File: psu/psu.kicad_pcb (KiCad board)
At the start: 2 copper layers, 100 x 100 mm, 134 parts, among them IC101 TSR 1-24150, IC102 STM32F334K8T6, IC103 TSR 1-2450, IC104 NCP161, IC201 INA139, IC202 AD8605, IC203 MCP1416, IC204 AD8065, IC205 INA139, IC206 AD8605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

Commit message: More PCB
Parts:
- moved C223 9.89 mm to (175.5, 103.8), turned to 270 degrees
- moved R228 9.39 mm to (180.0, 100.0), turned to 180 degrees
- moved C224 8.07 mm to (177.2, 103.8), turned to 270 degrees
- moved TP205 5.40 mm to (178.5, 114.8)
- moved IC205 5.01 mm to (180.0, 103.8), turned to 90 degrees
- moved D101 1.00 mm to (112.0, 122.0)
- moved D109 1.00 mm to (189.0, 120.0)
- moved D110 1.00 mm to (189.0, 123.0)
- moved D111 1.00 mm to (189.0, 126.5)
- moved R109 1.00 mm to (186.5, 125.5)
- moved R110 1.00 mm to (189.0, 121.5)
- moved R111 1.00 mm to (189.0, 124.5)
- moved D112 0.50 mm to (185.0, 133.5)
- moved D113 0.50 mm to (185.0, 135.0)
- moved D114 0.50 mm to (185.0, 138.0)
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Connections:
- net Net-(C223-Pad2) renamed /Flyback/390V
- TP205 pad 1: Net-(C227-Pad1) -> /I_OUT
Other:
- outline, holes or cut-outs redrawn
- board text added: "+"
- board text added: "-"
- board text added: "0V"
- board text added: "15V"
- board text added: "2019-08-27 r1 AG"
- board text added: "24V"
- board text added: "24V ~EN~ TX 0V"
- board text added: "24VDC 2.5A"
- board text added: "3V TX RX 0V"
- board text added: "3V3"
- board text added: "400V"
- board text added: "400V HV PSU"
- board text added: "5V"
- board text added: "CTRL"
- board text added: "Capacitors remain energised up to 1min after disconnection. Ensure they are discharged!"
- board text added: "ERR"
- board text added: "GD"
- board text added: "HIGH VOLTAGE"
- board text added: "IIN"
- board text added: "IOUT"
- board text added: "IQ"
- board text added: "VOUT"
- board text added: "VQ"

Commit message: More pcb layout
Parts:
- added G***: LOGO, psu:hv, F.Cu at (196.0, 95.0)
- added G***: LOGO, psu:hv, F.Cu at (196.0, 124.0)
- TP102, TP202, TP203, TP206, TP207: footprint agg:SIL-254P-01 -> agg:KEYSTONE5016
- moved C103 97.2 mm to (129.5, 66.0), turned to 270 degrees
- moved C104 95.6 mm to (124.2, 67.5), turned to 90 degrees
- moved Y101 93.7 mm to (127.0, 66.0), turned to 270 degrees
- moved D103 93.2 mm to (161.5, 61.5)
- moved R101 93.2 mm to (161.5, 57.5)
- moved TP101 93.2 mm to (161.5, 54.5)
- moved TP102 93.2 mm to (156.5, 57.5), turned to 180 degrees
- moved D104 93.1 mm to (166.2, 61.5)
- moved R104 93.1 mm to (166.2, 57.5)
- moved TP103 93.1 mm to (166.2, 54.5)
- moved D105 93.0 mm to (171.0, 61.5)
- moved R105 93.0 mm to (171.0, 57.5)
- moved TP104 93.0 mm to (171.0, 54.5)
- moved D108 92.9 mm to (175.8, 61.5)
- moved R108 92.9 mm to (175.8, 57.5)
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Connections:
- TP202 pad 1: /GD -> Net-(IC203-Pad5)
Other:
- outline, holes or cut-outs redrawn
- board text added: "Capacitors remain energised up to 1min after disconnection."
- board text removed: "CTRL"
- board text removed: "Capacitors remain energised up to 1min after disconnection. Ensure they are discharged!"

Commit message: routing
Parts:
- moved R102 58.5 mm to (107.0, 91.0), turned to 0 degrees
- moved R103 55.8 mm to (107.0, 89.0), turned to 180 degrees
- moved C101 52.4 mm to (109.5, 90.0), turned to 270 degrees
- moved J103 4.00 mm to (195.2, 132.0)
- moved D204 2.06 mm to (185.5, 126.5)
- moved D205 2.06 mm to (189.0, 126.5)
- moved D103 1.75 mm to (161.5, 63.2)
- moved D104 1.75 mm to (166.2, 63.2)
- moved D105 1.75 mm to (171.0, 63.2)
- moved D106 1.75 mm to (185.2, 63.2)
- moved D107 1.75 mm to (180.5, 63.0)
- moved D108 1.75 mm to (175.8, 63.2)
- moved R101 1.75 mm to (161.5, 59.2)
- moved R104 1.75 mm to (166.2, 59.2)
- moved R105 1.75 mm to (171.0, 59.2)
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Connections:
- net Net-(C216-Pad2) renamed /Flyback/400V
- IC102 pad 12: /VQ -> /V_Q
- IC102 pad 14: /VQ -> /V_Q
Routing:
- net GND: track 0.00 -> 258.7 mm, vias 0 -> 86
- net 24v: track 0.00 -> 156.4 mm
- net 3v3: track 0.00 -> 101.4 mm
- net /I_OUT: track 0.00 -> 85.4 mm
- net Net-(C206-Pad2): track 0.00 -> 72.8 mm
- net Net-(C214-Pad2): track 0.00 -> 62.0 mm
- net /Flyback/400V: track 0.00 -> 58.6 mm
- net /V_Q: track 0.00 -> 52.1 mm
- net /I_Q: track 0.00 -> 42.5 mm
- net /I_IN: track 0.00 -> 39.7 mm
- net /Flyback/390V: track 0.00 -> 35.8 mm, vias 0 -> 2
- net /VIN_MON: track 0.00 -> 30.6 mm
- net 5v: track 0.00 -> 30.0 mm
- net Net-(D101-Pad1): track 0.00 -> 23.4 mm
- net /Flyback/HV+: track 0.00 -> 20.8 mm
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- added copper zone on B.Cu, net GND
- added copper zone on F.Cu, net GND
- added copper zone on F.Cu, net Net-(C206-Pad2)
- added copper zone on F.Cu, net Net-(C214-Pad2)
- added copper zone on F.Cu, net Net-(Q201-PadS)
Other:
- outline, holes or cut-outs redrawn
- rule trace_min: 0.2 -> 0.15
- rule via_min_size: 0.4 -> 0.6

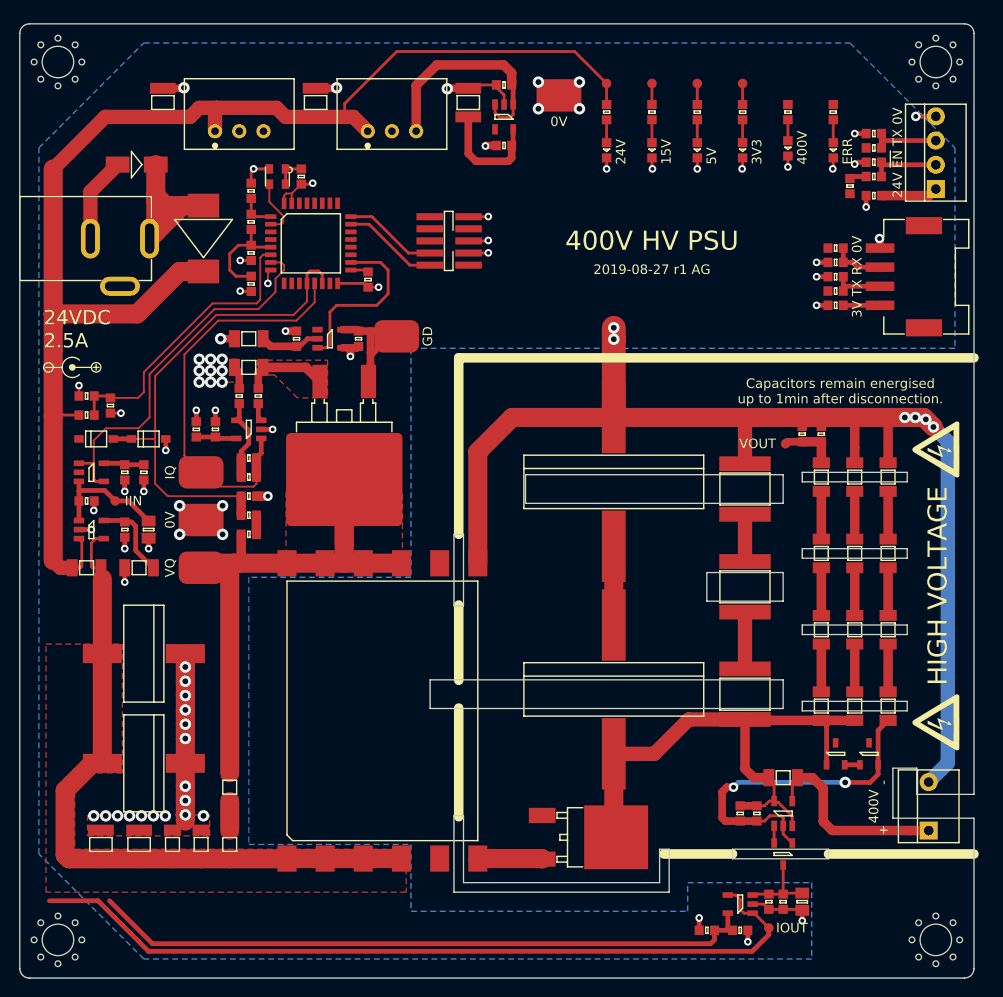
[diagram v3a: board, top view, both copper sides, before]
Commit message: Complete routing. But maybe the transformer is the wrong way around.
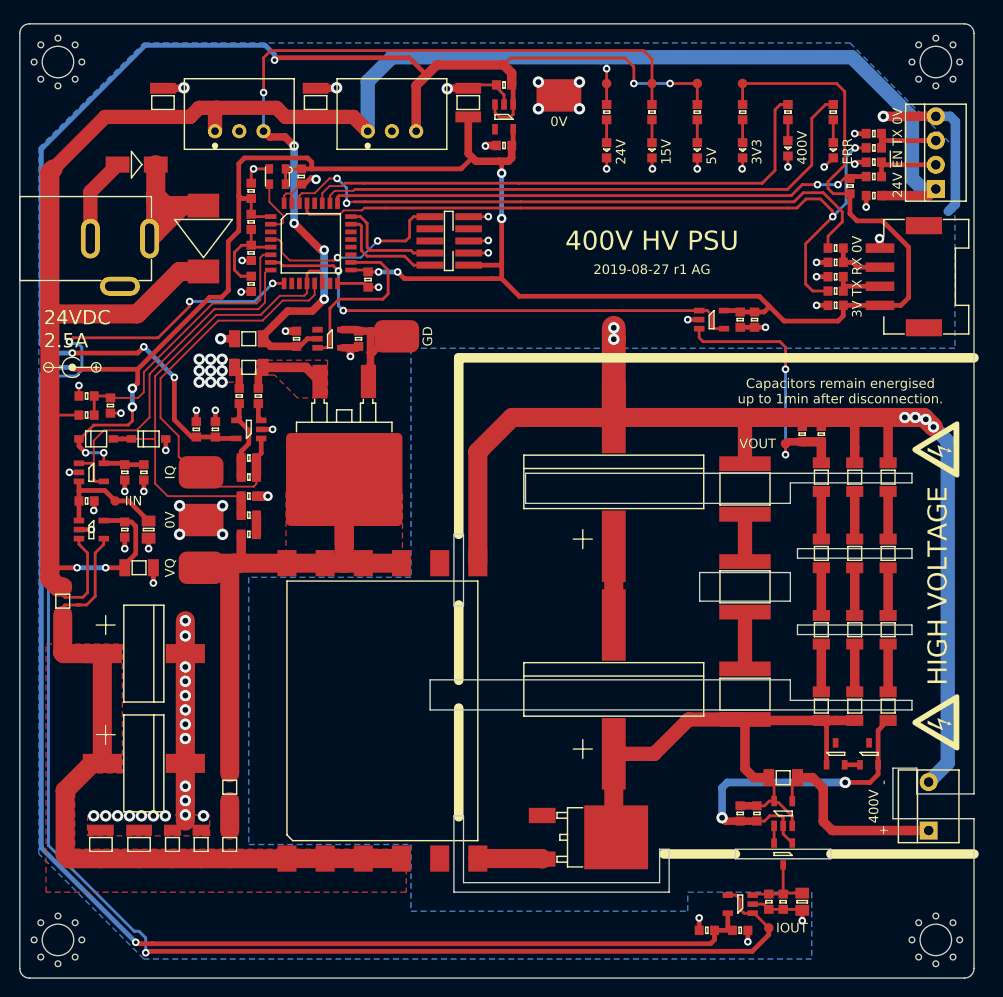
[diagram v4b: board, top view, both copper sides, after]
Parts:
- added C228: 100n, agg:0603, F.Cu at (175.5, 81.0)
- added C229: 1µ, agg:0603, F.Cu at (177.0, 81.0)
- added IC207: AD8605, agg:SOT-23-5, F.Cu at (172.5, 81.0)
- moved C214 6.00 mm to (122.0, 136.0)
- moved R204 6.00 mm to (122.0, 130.0)
- moved R201 4.30 mm to (104.5, 110.5), turned to 270 degrees
- turned C201 to 0 degrees
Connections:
- C214 pad 1: Net-(C214-Pad1) -> Net-(C206-Pad2)
- C222 pad 1: /VOUT_MON -> Net-(C222-Pad1)
- IC102 pad 26: /LED_STAT -> /LED_FAULT
- IC102 pad 27: /LED_FAULT -> /LED_STAT
- IC102 pad 7: /I_IN -> /VOUT_MON
- IC102 pad 8: /VOUT_MON -> /I_IN
- Q201 pad D: Net-(C214-Pad2) -> Net-(Q201-PadD)
- R204 pad 1: Net-(C206-Pad2) -> Net-(C214-Pad2)
- R204 pad 2: Net-(C214-Pad1) -> Net-(Q201-PadD)
- R206 pad 1: Net-(C214-Pad2) -> Net-(Q201-PadD)
- R216 pad 2: /VOUT_MON -> Net-(C222-Pad1)
- R217 pad 1: /VOUT_MON -> Net-(C222-Pad1)
- T201 pad 10: Net-(C214-Pad2) -> Net-(Q201-PadD)
- T201 pad 11: Net-(C214-Pad2) -> Net-(Q201-PadD)
- T201 pad 12: Net-(C214-Pad2) -> Net-(Q201-PadD)
- T201 pad 9: Net-(C214-Pad2) -> Net-(Q201-PadD)
- TP204 pad 1: /VOUT_MON -> Net-(C222-Pad1)
- TP207 pad 1: Net-(C214-Pad2) -> Net-(Q201-PadD)
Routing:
- net 3v3: track 101.4 -> 360.0 mm, vias 0 -> 10
- net 5v: track 30.0 -> 143.3 mm, vias 0 -> 6
- net /I_OUT: track 85.4 -> 170.9 mm, vias 0 -> 4
- net 15v: track 8.56 -> 90.0 mm, vias 0 -> 5
- net /UART_TX: track 0.00 -> 78.1 mm, vias 0 -> 2
- net /UART_RX: track 0.00 -> 66.2 mm, vias 0 -> 2
- net Net-(Q201-PadD): track 0.00 -> 62.0 mm
- net 24v: track 156.4 -> 217.0 mm, vias 0 -> 3
- net /LED_FAULT: track 0.00 -> 60.4 mm
- net Net-(C214-Pad2): track 62.0 -> 3.00 mm
- net /LED_STAT: track 0.00 -> 57.4 mm
- net /~RUN: track 1.78 -> 56.9 mm, vias 0 -> 2
- net /VOUT_MON: track 7.56 -> 53.2 mm, vias 1 -> 2
- net Net-(C222-Pad1): track 0.00 -> 28.8 mm, vias 0 -> 2
- net GND: track 258.7 -> 283.1 mm, vias 86 -> 91
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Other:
- outline, holes or cut-outs redrawn
- net class MV added: clearance 0.35, trace_width 0.25, via_dia 0.8, via_drill 0.4
- rule pad_to_mask_clearance: 0.051 -> 0.03

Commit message: Complete routing take 2, with transformer secondary pins swapped
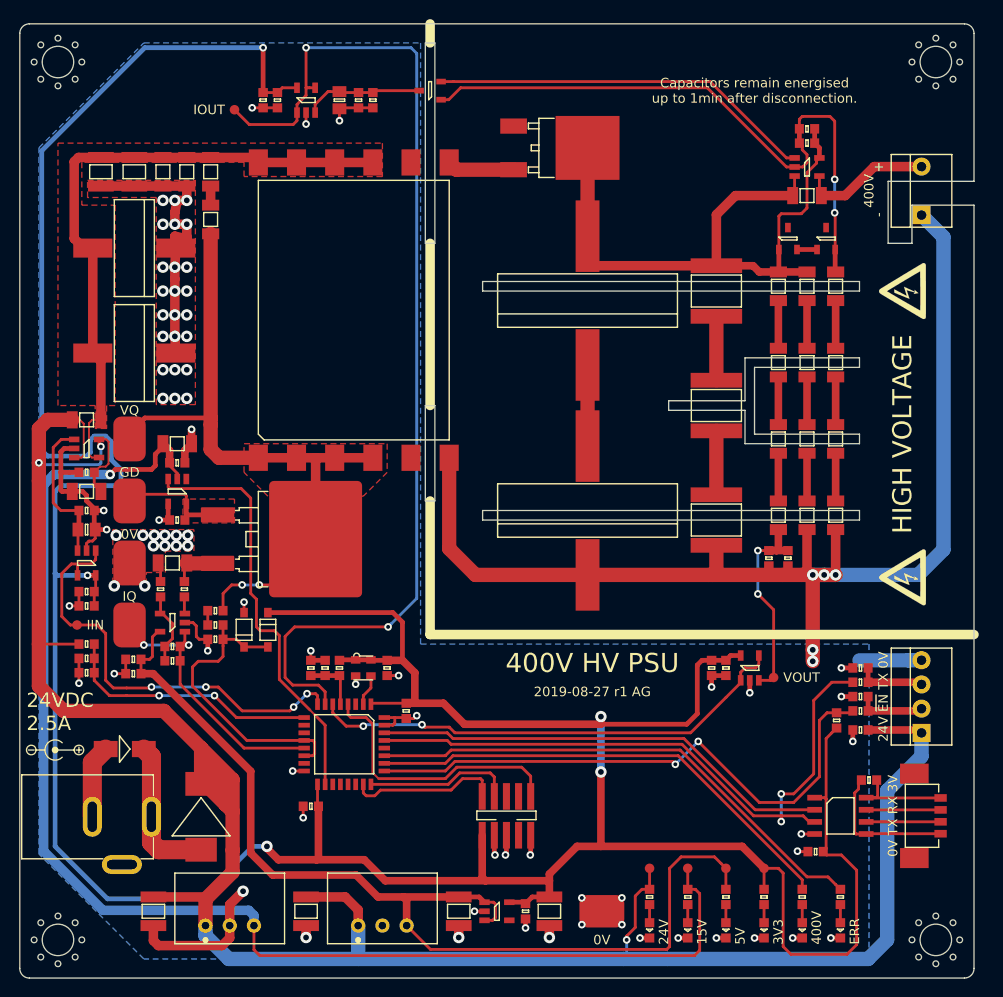
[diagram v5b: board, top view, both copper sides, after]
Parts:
- removed D112, D113, D114: ESD_DIODE, agg:0603
- removed G*** (x2): LOGO, psu:hv
- removed R112, R113: 1k, agg:0603
- added C112: 100n, agg:0603, F.Cu at (183.4, 136.8)
- added C113: 100n, agg:0603, F.Cu at (189.0, 129.2)
- added IC105: ADuM1201, agg:SOIC-8, F.Cu at (186.0, 133.0)
- added X106: HV SIGN, psu:hv, F.Cu at (192.5, 78.0)
- added X107: HV SIGN, psu:hv, F.Cu at (192.5, 108.0)
- C110: value 1µ -> 10µ; footprint agg:0603 -> agg:1210
- J104: footprint agg:SM04B-PASS -> agg:MOLEX-PICOBLADE-53398-0471
- moved TP205 102.4 mm to (122.5, 59.0)
- moved C226 100.3 mm to (125.5, 58.0), turned to 270 degrees
- moved C225 97.9 mm to (127.0, 58.0), turned to 270 degrees
- moved C227 97.0 mm to (133.5, 58.0)
- moved IC206 95.8 mm to (130.0, 58.0), turned to 90 degrees
- moved R227 95.1 mm to (135.5, 58.0)
- moved R226 93.7 mm to (137.0, 58.0)
- moved Q202 88.1 mm to (143.0, 57.0), turned to 180 degrees
- moved C110 86.7 mm to (146.0, 143.0), turned to 270 degrees
- moved TP102 85.6 mm to (161.0, 143.0), turned to 0 degrees
- moved C102 85.2 mm to (155.5, 143.0), turned to 270 degrees
- moved C106 84.8 mm to (114.0, 143.0), turned to 270 degrees
- moved C109 84.8 mm to (130.0, 143.0), turned to 270 degrees
- moved IC101 83.3 mm to (122.0, 144.5)
- moved IC103 83.3 mm to (138.0, 144.5)
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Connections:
- IC102 pad 26: /LED_FAULT -> /LED_STAT
- IC102 pad 27: /LED_STAT -> /LED_FAULT
- IC102 pad 6: /VIN_MON -> /VOUT_MON
- IC102 pad 7: /VOUT_MON -> /I_OUT
- IC102 pad 9: /I_OUT -> /VIN_MON
- J103 pad 1: /Flyback/HV+ -> GND
- J103 pad 3: GND -> /Flyback/HV+
- J104 pad 1: 3v3 -> Net-(C113-Pad1)
- J104 pad 4: GND -> Net-(C113-Pad2)
- T201 pad 1: Net-(C206-Pad2) -> Net-(Q201-PadD)
- T201 pad 10: Net-(Q201-PadD) -> Net-(C206-Pad2)
- T201 pad 11: Net-(Q201-PadD) -> Net-(C206-Pad2)
- T201 pad 12: Net-(Q201-PadD) -> Net-(C206-Pad2)
- T201 pad 2: Net-(C206-Pad2) -> Net-(Q201-PadD)
- T201 pad 3: Net-(C206-Pad2) -> Net-(Q201-PadD)
- T201 pad 4: Net-(C206-Pad2) -> Net-(Q201-PadD)
- T201 pad 6: Net-(D203-Pad2) -> GND
- T201 pad 7: GND -> Net-(D203-Pad2)
- T201 pad 9: Net-(Q201-PadD) -> Net-(C206-Pad2)
- TP201 pad 1: Net-(C205-Pad1) -> /I_IN
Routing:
- net /I_OUT: track 170.9 -> 111.2 mm, vias 4 -> 2
- net 15v: track 90.0 -> 143.1 mm, vias 5 -> 1
- net Net-(IC205-Pad1): track 1.80 -> 40.4 mm
- net 5v: track 143.3 -> 109.9 mm, vias 6 -> 0
- net /Flyback/390V: track 36.1 -> 67.2 mm
- net 24v: track 217.0 -> 244.1 mm
- net /GD: track 18.7 -> 44.1 mm
- net /V_Q: track 51.5 -> 31.6 mm
- net /UART_RX: track 66.2 -> 48.4 mm, vias 2 -> 0
- net Net-(C113-Pad2): track 0.00 -> 14.9 mm
- net 3v3: track 360.0 -> 373.8 mm, vias 10 -> 5
- net /I_Q: track 42.7 -> 29.9 mm, vias 0 -> 2
- net Net-(C206-Pad2): track 78.4 -> 66.3 mm
- net Net-(C113-Pad1): track 0.00 -> 10.8 mm
- net /I_IN: track 37.3 -> 46.4 mm, vias 0 -> 4
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- added copper zone on F.Cu, net Net-(IC203-Pad5)
- added copper zone on F.Cu, net Net-(Q201-PadD)
- removed copper zone on F.Cu, net Net-(C214-Pad2)
- removed copper zone on F.Cu, net Net-(Q201-PadS)
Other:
- outline, holes or cut-outs redrawn
- net class Default: clearance 0.2 -> 0.25
- rule trace_clearance: 0.2 -> 0.25
- board text added: "0V TX RX 3V"
- board text removed: "3V TX RX 0V"

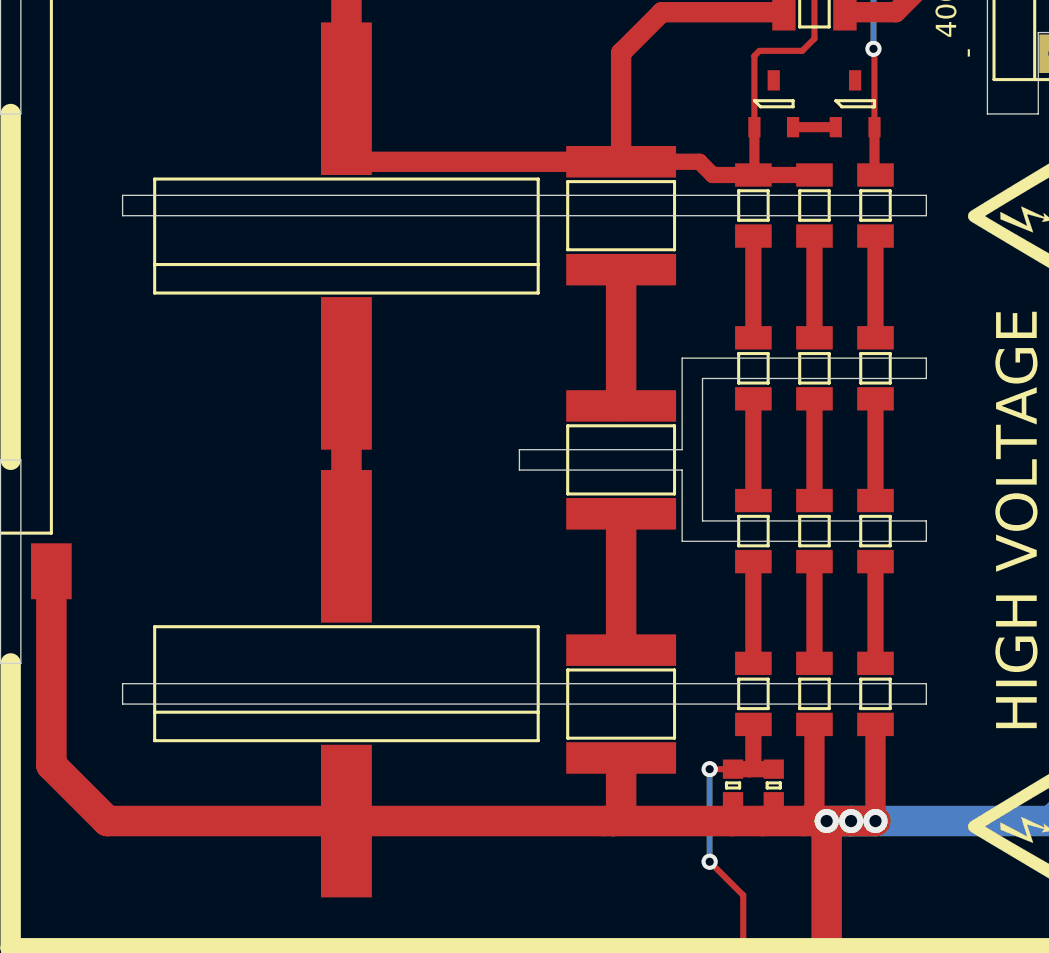
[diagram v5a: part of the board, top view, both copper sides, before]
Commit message: Reposition HV resistor chains
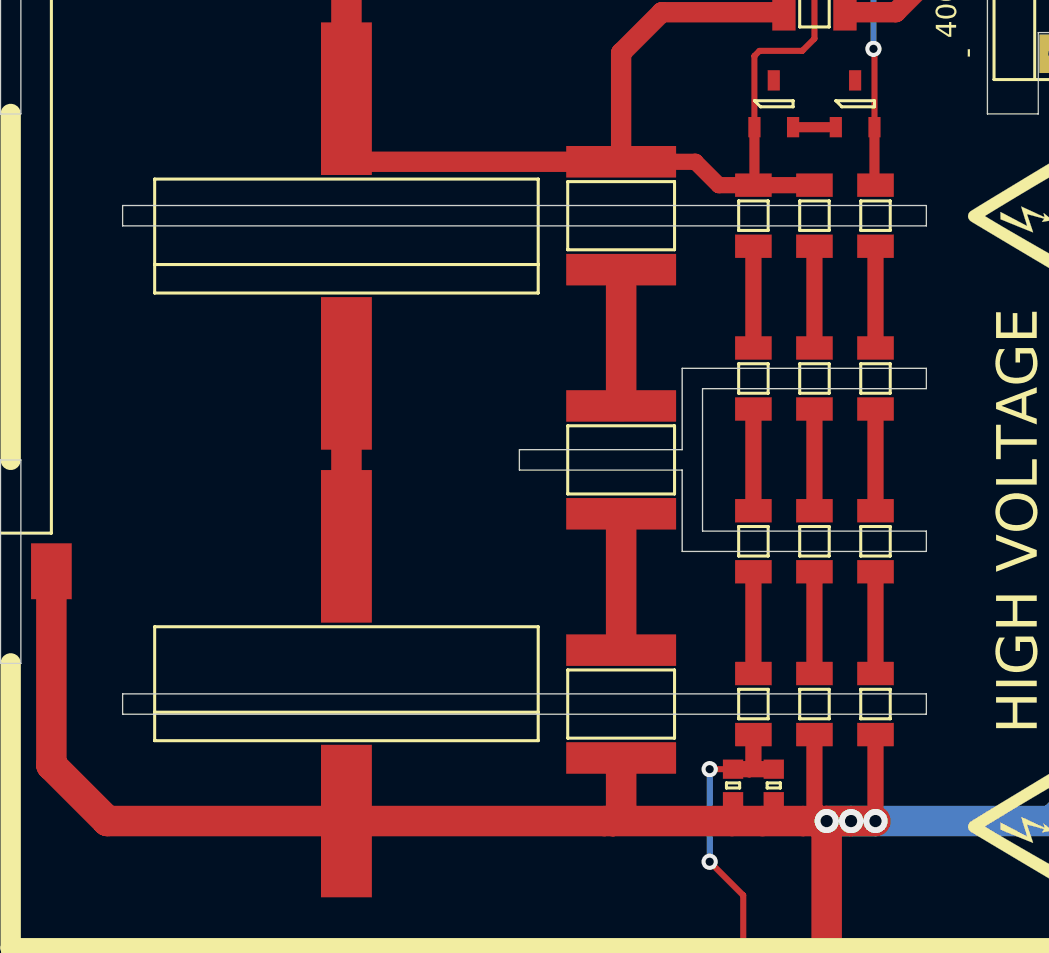
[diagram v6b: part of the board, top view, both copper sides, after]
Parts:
- moved R213 0.50 mm to (179.5, 78.0)
- moved R214 0.50 mm to (179.5, 86.0)
- moved R215 0.50 mm to (179.5, 94.0)
- moved R216 0.50 mm to (179.5, 102.0)
- moved R218 0.50 mm to (182.5, 78.0)
- moved R219 0.50 mm to (182.5, 86.0)
- moved R220 0.50 mm to (182.5, 94.0)
- moved R221 0.50 mm to (182.5, 102.0)
- moved R222 0.50 mm to (185.5, 78.0)
- moved R223 0.50 mm to (185.5, 86.0)
- moved R224 0.50 mm to (185.5, 94.0)
- moved R225 0.50 mm to (185.5, 102.0)
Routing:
- net GND: track 277.3 -> 276.3 mm
- net /Flyback/400V: track 65.8 -> 66.5 mm
- net Net-(C222-Pad1): track 21.1 -> 20.6 mm
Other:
- outline, holes or cut-outs redrawn
